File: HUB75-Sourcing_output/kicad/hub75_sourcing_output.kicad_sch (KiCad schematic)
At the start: 9 parts, among them J13 Screw_Terminal_01x02, Q13 AO3401A, Q26 2N7002, U2 CL2N8-G

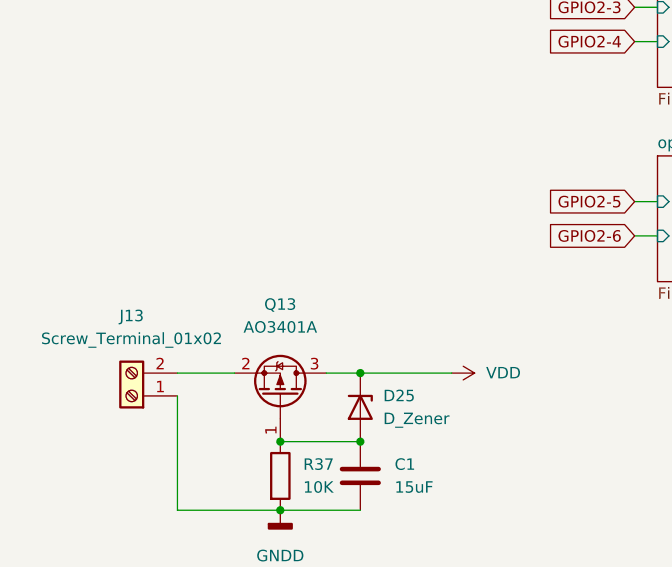
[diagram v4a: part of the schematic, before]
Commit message: New version after prototype failed
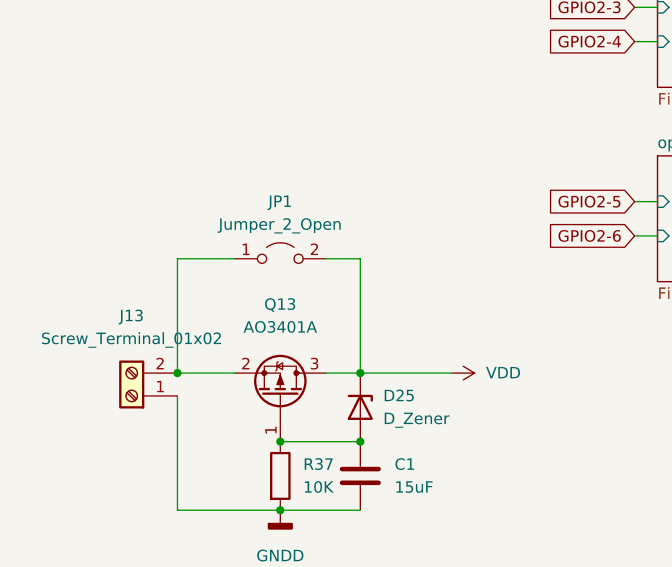
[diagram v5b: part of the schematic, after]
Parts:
- added JP1: Jumper_2_Open, Jumper:SolderJumper-2_P1.3mm_Open_TrianglePad1.0x1.5mm, symbol Jumper:Jumper_2_Open
- C1: footprint Capacitor_THT:C_Disc_D5.0mm_W2.5mm_P5.00mm -> Capacitor_SMD:C_1206_3216Metric_Pad1.33x1.80mm_HandSolder
- D25: footprint Diode_SMD:D_SOD-123 -> Diode_SMD:D_SOT-23_ANK
- HUB75-1, HUB75-2: footprint Connector_PinHeader_2.54mm:PinHeader_2x08_P2.54mm_Vertical -> Connector_IDC:IDC-Header_2x08_P2.54mm_Vertical
- R37: footprint Resistor_SMD:R_2010_5025Metric_Pad1.40x2.65mm_HandSolder -> Resistor_SMD:R_1206_3216Metric_Pad1.30x1.75mm_HandSolder
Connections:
- net VDD: now also JP1.2 (B)
- net at J13.2 (Pin_2), Q13.2 (S): now also JP1.1 (A)
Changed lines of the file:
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@@
   (junction (at 201.93 63.5) (diameter 0) (color 0 0 0 0)
   )
+  (junction (at 31.75 175.26) (diameter 0) (color 0 0 0 0)
+  )
   (junction (at 43.18 182.88) (diameter 0) (color 0 0 0 0)
   )
@@
     (stroke (width 0) (type default) (color 0 0 0 0))
   )
+  (wire (pts (xy 48.26 162.56) (xy 52.07 162.56))
+    (stroke (width 0) (type default) (color 0 0 0 0))
+  )
   (wire (pts (xy 201.93 63.5) (xy 205.74 63.5))
     (stroke (width 0) (type default) (color 0 0 0 0))
@@
     (stroke (width 0) (type default) (color 0 0 0 0))
   )
+  (wire (pts (xy 38.1 162.56) (xy 31.75 162.56))
+    (stroke (width 0) (type default) (color 0 0 0 0))
+  )
   (wire (pts (xy 52.07 175.26) (xy 62.23 175.26))
     (stroke (width 0) (type default) (color 0 0 0 0))
@@
     (stroke (width 0) (type default) (color 0 0 0 0))
   )
+  (wire (pts (xy 31.75 162.56) (xy 31.75 175.26))
+    (stroke (width 0) (type default) (color 0 0 0 0))
+  )
   (wire (pts (xy 82.55 58.42) (xy 85.09 58.42))
+    (stroke (width 0) (type default) (color 0 0 0 0))
+  )
+  (wire (pts (xy 52.07 162.56) (xy 52.07 175.26))
     (stroke (width 0) (type default) (color 0 0 0 0))
   )
@@
       (effects (font (size 1.27 1.27)) (justify left))
     )
-    (property "Footprint" "Resistor_SMD:R_2010_5025Metric_Pad1.40x2.65mm_HandSolder" (id 2) (at 41.402 186.69 90)
+    (property "Footprint" "Resistor_SMD:R_1206_3216Metric_Pad1.30x1.75mm_HandSolder" (id 2) (at 41.402 186.69 90)
       (effects (font (size 1.27 1.27)) hide)
     )
@@
     (pin "1")
   )
+  (symbol (lib_id "Jumper:Jumper_2_Open") (at 43.18 162.56 0) (unit 1)
+    (in_bom yes) (on_board yes) (fields_autoplaced)
+    (property "Reference" "JP1" (id 0) (at 43.18 156.21 0))
+    (property "Value" "Jumper_2_Open" (id 1) (at 43.18 158.75 0))
+    (property "Footprint" "Jumper:SolderJumper-2_P1.3mm_Open_TrianglePad1.0x1.5mm" (id 2) (at 43.18 162.56 0)
+      (effects (font (size 1.27 1.27)) hide)
+    )
+    (property "Datasheet" "~" (id 3) (at 43.18 162.56 0)
+      (effects (font (size 1.27 1.27)) hide)
+    )
+    (pin "1")
+    (pin "2")
+  )
   (symbol (lib_id "Device:C") (at 52.07 186.69 0) (unit 1)
     (in_bom yes) (on_board yes) (fields_autoplaced)
@@
       (effects (font (size 1.27 1.27)) (justify left))
     )
-    (property "Footprint" "Capacitor_THT:C_Disc_D5.0mm_W2.5mm_P5.00mm" (id 2) (at 53.0352 190.5 0)
+    (property "Footprint" "Capacitor_SMD:C_1206_3216Metric_Pad1.33x1.80mm_HandSolder" (id 2) (at 53.0352 190.5 0)
       (effects (font (size 1.27 1.27)) hide)
     )
@@
       (effects (font (size 1.27 1.27)) (justify left))
     )
-    (property "Footprint" "Diode_SMD:D_SOD-123" (id 2) (at 52.07 179.07 0)
+    (property "Footprint" "Diode_SMD:D_SOT-23_ANK" (id 2) (at 52.07 179.07 0)
       (effects (font (size 1.27 1.27)) hide)
     )
@@
     (property "Reference" "HUB75-2" (id 0) (at 36.83 104.14 0))
     (property "Value" "Conn_02x08_Odd_Even" (id 1) (at 36.83 106.68 0))
-    (property "Footprint" "Connector_PinHeader_2.54mm:PinHeader_2x08_P2.54mm_Vertical" (id 2) (at 35.56 118.11 0)
-      (effects (font (size 1.27 1.27)) hide)
+    (property "Footprint" "Connector_IDC:IDC-Header_2x08_P2.54mm_Vertical" (id 2) (at 35.56 118.11 0)
+      (effects (font (size 0 0)) hide)
     )
     (property "Datasheet" "~" (id 3) (at 35.56 118.11 0)
@@
     (property "Reference" "HUB75-1" (id 0) (at 36.83 26.67 0))
     (property "Value" "Conn_02x08_Odd_Even" (id 1) (at 36.83 29.21 0))
-    (property "Footprint" "Connector_PinHeader_2.54mm:PinHeader_2x08_P2.54mm_Vertical" (id 2) (at 35.56 40.64 0)
+    (property "Footprint" "Connector_IDC:IDC-Header_2x08_P2.54mm_Vertical" (id 2) (at 35.56 40.64 0)
       (effects (font (size 1.27 1.27)) hide)
     )
@@
       (reference "#PWR0104") (unit 1) (value "VDD") (footprint "")
     )
+    (path "/7134724f-277a-4c58-bbec-7ceaf30b9ed0/0b270438-67c5-4f5c-ae5a-99e8156324e0"
+      (reference "#PWR0105") (unit 1) (value "GNDD") (footprint "")
+    )
+    (path "/b97ce019-f40c-494d-a8f2-c1e1e7770eda/0b270438-67c5-4f5c-ae5a-99e8156324e0"
+      (reference "#PWR0106") (unit 1) (value "GNDD") (footprint "")
+    )
+    (path "/6b06ee6c-43d0-46ea-805d-1eaf19e0c0d6/0b270438-67c5-4f5c-ae5a-99e8156324e0"
+      (reference "#PWR0107") (unit 1) (value "GNDD") (footprint "")
+    )
+    (path "/4a805342-0b43-48e9-8386-b9afd15cb415/0b270438-67c5-4f5c-ae5a-99e8156324e0"
+      (reference "#PWR0108") (unit 1) (value "GNDD") (footprint "")
+    )
+    (path "/af8f1dfd-4712-4978-9db1-fbab7159693f/0b270438-67c5-4f5c-ae5a-99e8156324e0"
+      (reference "#PWR0109") (unit 1) (value "GNDD") (footprint "")
+    )
+    (path "/a07fb6ac-465b-4261-9707-bed709ee7e00/0b270438-67c5-4f5c-ae5a-99e8156324e0"
+      (reference "#PWR0110") (unit 1) (value "GNDD") (footprint "")
+    )
     (path "/41f443e3-4851-44e4-bb91-0aa8ef1d1460"
-      (reference "C1") (unit 1) (value "15uF") (footprint "Capacitor_THT:C_Disc_D5.0mm_W2.5mm_P5.00mm")
+      (reference "C1") (unit 1) (value "15uF") (footprint "Capacitor_SMD:C_1206_3216Metric_Pad1.33x1.80mm_HandSolder")
     )
     (path "/7134724f-277a-4c58-bbec-7ceaf30b9ed0/73d50809-198d-421c-ba1f-67bbf2431c0c/a824993b-7dab-4227-a94b-9a29e7d7d5ec"
@@
     )
     (path "/b7471806-38d2-4dfc-91b0-dc021e073a52"
-      (reference "D25") (unit 1) (value "D_Zener") (footprint "Diode_SMD:D_SOD-123")
+      (reference "D25") (unit 1) (value "D_Zener") (footprint "Diode_SMD:D_SOT-23_ANK")
     )
     (path "/e9910004-58a5-4527-b24d-c5f137185cc9"
-      (reference "HUB75-1") (unit 1) (value "Conn_02x08_Odd_Even") (footprint "Connector_PinHeader_2.54mm:PinHeader_2x08_P2.54mm_Vertical")
+      (reference "HUB75-1") (unit 1) (value "Conn_02x08_Odd_Even") (footprint "Connector_IDC:IDC-Header_2x08_P2.54mm_Vertical")
     )
     (path "/dbf80ebe-7eb2-4560-8bdb-30e3608dd7c9"
-      (reference "HUB75-2") (unit 1) (value "Conn_02x08_Odd_Even") (footprint "Connector_PinHeader_2.54mm:PinHeader_2x08_P2.54mm_Vertical")
+      (reference "HUB75-2") (unit 1) (value "Conn_02x08_Odd_Even") (footprint "Connector_IDC:IDC-Header_2x08_P2.54mm_Vertical")
     )
     (path "/7134724f-277a-4c58-bbec-7ceaf30b9ed0/73d50809-198d-421c-ba1f-67bbf2431c0c/d27d4a04-d41d-4d25-b024-2f07bf9acf32"
@@
       (reference "J13") (unit 1) (value "Screw_Terminal_01x02") (footprint "TerminalBlock_Phoenix:TerminalBlock_Phoenix_PT-1,5-2-3.5-H_1x02_P3.50mm_Horizontal")
     )
+    (path "/24539bbd-2ab6-42e4-8bae-55a24587c281"
+      (reference "JP1") (unit 1) (value "Jumper_2_Open") (footprint "Jumper:SolderJumper-2_P1.3mm_Open_TrianglePad1.0x1.5mm")
+    )
     (path "/7134724f-277a-4c58-bbec-7ceaf30b9ed0/73d50809-198d-421c-ba1f-67bbf2431c0c/76c391d7-ee48-4fc3-9f76-96df5a10ea37"
       (reference "Q1") (unit 1) (value "BSS84") (footprint "Package_TO_SOT_SMD:SOT-23")
@@
     )
     (path "/0be1527b-c337-4d05-9af1-4ecaa2fb462c"
-      (reference "R37") (unit 1) (value "10K") (footprint "Resistor_SMD:R_2010_5025Metric_Pad1.40x2.65mm_HandSolder")
+      (reference "R37") (unit 1) (value "10K") (footprint "Resistor_SMD:R_1206_3216Metric_Pad1.30x1.75mm_HandSolder")
     )
     (path "/7134724f-277a-4c58-bbec-7ceaf30b9ed0/73d50809-198d-421c-ba1f-67bbf2431c0c/dc8c3685-7386-4495-b106-4383852f2abf"
